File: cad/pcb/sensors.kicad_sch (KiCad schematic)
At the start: 0 parts

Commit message: finish mcu connections
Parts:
- added IC?: MXC4005XC, MXC4005XC, symbol Gyroscope:MXC4005XC
- added IC?: PI4IOE5V96224ZLEX, QFN40P300X600X80-33N, symbol I/O Expander:PI4IOE5V96224ZLEX
- added Q?: 1541201NEA400, 1541201NEA400, symbol Phototransistor:1541201NEA400
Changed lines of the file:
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@@
     (comment 4 "Simon Brenninger")
   )
+  (symbol (lib_id "Phototransistor:1541201NEA400") (at 50.8 49.53 0) (unit 1)
+    (in_bom yes) (on_board yes) (fields_autoplaced)
+    (property "Reference" "Q?" (id 0) (at 54.61 55.6259 0)
+      (effects (font (size 1.27 1.27)) (justify left))
+    )
+    (property "Value" "1541201NEA400" (id 1) (at 54.61 58.1659 0)
+      (effects (font (size 1.27 1.27)) (justify left))
+    )
+    (property "Footprint" "1541201NEA400" (id 2) (at 54.61 60.96 0)
+      (effects (font (size 1.27 1.27)) (justify left) hide)
+    )
+    (property "Datasheet" "https://www.mouser.dk/datasheet/2/445/1541201NEA400-1715480.pdf" (id 3) (at 54.61 63.5 0)
+      (effects (font (size 1.27 1.27)) (justify left) hide)
+    )
+    (property "Description" "WURTH ELEKTRONIK - 1541201NEA400 - Phototransistor, 940 nm, 140 , 150 mW, 2 Pins, 1206, WL-STCB Series" (id 4) (at 54.61 66.04 0)
+      (effects (font (size 1.27 1.27)) (justify left) hide)
+    )
+    (property "Height" "1.2" (id 5) (at 54.61 68.58 0)
+      (effects (font (size 1.27 1.27)) (justify left) hide)
+    )
+    (property "Mouser Part Number" "710-1541201NEA400" (id 6) (at 54.61 71.12 0)
+      (effects (font (size 1.27 1.27)) (justify left) hide)
+    )
+    (property "Mouser Price/Stock" "https://www.mouser.co.uk/ProductDetail/Wurth-Elektronik/1541201NEA400?qs=u16ybLDytRZ%252BRXqtXC1wNA%3D%3D" (id 7) (at 54.61 73.66 0)
+      (effects (font (size 1.27 1.27)) (justify left) hide)
+    )
+    (property "Manufacturer_Name" "Wurth Elektronik" (id 8) (at 54.61 76.2 0)
+      (effects (font (size 1.27 1.27)) (justify left) hide)
+    )
+    (property "Manufacturer_Part_Number" "1541201NEA400" (id 9) (at 54.61 78.74 0)
+      (effects (font (size 1.27 1.27)) (justify left) hide)
+    )
+    (pin "1")
+    (pin "2")
+  )
+  (symbol (lib_id "Gyroscope:MXC4005XC") (at 40.64 93.98 0) (unit 1)
+    (in_bom yes) (on_board yes) (fields_autoplaced)
+    (property "Reference" "IC?" (id 0) (at 53.34 86.36 0))
+    (property "Value" "MXC4005XC" (id 1) (at 53.34 88.9 0))
+    (property "Footprint" "MXC4005XC" (id 2) (at 62.23 91.44 0)
+      (effects (font (size 1.27 1.27)) (justify left) hide)
+    )
+    (property "Datasheet" "https://datasheet.datasheetarchive.com/originals/distributors/Datasheets_SAMA/aa0fcdfc55209a6ab2215b00180fe2f1.pdf" (id 3) (at 62.23 93.98 0)
+      (effects (font (size 1.27 1.27)) (justify left) hide)
+    )
+    (property "Description" "Accelerometers Monolithic and Wafer Level Packaged Three-Axis Accelerometer" (id 4) (at 62.23 96.52 0)
+      (effects (font (size 1.27 1.27)) (justify left) hide)
+    )
+    (property "Height" "0.885" (id 5) (at 62.23 99.06 0)
+      (effects (font (size 1.27 1.27)) (justify left) hide)
+    )
+    (property "Mouser Part Number" "438-MXC4005XC" (id 6) (at 62.23 101.6 0)
+      (effects (font (size 1.27 1.27)) (justify left) hide)
+    )
+    (property "Mouser Price/Stock" "https://www.mouser.co.uk/ProductDetail/MEMSIC/MXC4005XC?qs=RcG8xmE7yp3iyYgWLmAtUw%3D%3D" (id 7) (at 62.23 104.14 0)
+      (effects (font (size 1.27 1.27)) (justify left) hide)
+    )
+    (property "Manufacturer_Name" "MEMSIC" (id 8) (at 62.23 106.68 0)
+      (effects (font (size 1.27 1.27)) (justify left) hide)
+    )
+    (property "Manufacturer_Part_Number" "MXC4005XC" (id 9) (at 62.23 109.22 0)
+      (effects (font (size 1.27 1.27)) (justify left) hide)
+    )
+    (pin "1")
+    (pin "2")
+    (pin "3")
+    (pin "4")
+    (pin "5")
+    (pin "6")
+  )
+  (symbol (lib_id "I{slash}O Expander:PI4IOE5V96224ZLEX") (at 180.34 63.5 0) (unit 1)
+    (in_bom yes) (on_board yes) (fields_autoplaced)
+    (property "Reference" "IC?" (id 0) (at 202.6794 104.14 0)
+      (effects (font (size 1.27 1.27)) (justify left))
+    )
+    (property "Value" "PI4IOE5V96224ZLEX" (id 1) (at 202.6794 106.68 0)
+      (effects (font (size 1.27 1.27)) (justify left))
+    )
+    (property "Footprint" "QFN40P300X600X80-33N" (id 2) (at 209.55 53.34 0)
+      (effects (font (size 1.27 1.27)) (justify left) hide)
+    )
+    (property "Datasheet" "https://www.diodes.com/assets/Datasheets/PI4IOE5V96224.pdf" (id 3) (at 209.55 55.88 0)
+      (effects (font (size 1.27 1.27)) (justify left) hide)
+    )
+    (property "Description" "Interface - I/O Expanders 24-bit I2C-bus I/O Expander" (id 4) (at 209.55 58.42 0)
+      (effects (font (size 1.27 1.27)) (justify left) hide)
+    )
+    (property "Height" "0.8" (id 5) (at 209.55 60.96 0)
+      (effects (font (size 1.27 1.27)) (justify left) hide)
+    )
+    (property "Mouser Part Number" "729-I4IOE5V96224ZLEX" (id 6) (at 209.55 63.5 0)
+      (effects (font (size 1.27 1.27)) (justify left) hide)
+    )
+    (property "Mouser Price/Stock" "https://www.mouser.co.uk/ProductDetail/Diodes-Incorporated/PI4IOE5V96224ZLEX?qs=0lQeLiL1qybZKU%252B6WN8aKg%3D%3D" (id 7) (at 209.55 66.04 0)
+      (effects (font (size 1.27 1.27)) (justify left) hide)
+    )
+    (property "Manufacturer_Name" "Diodes Inc." (id 8) (at 209.55 68.58 0)
+      (effects (font (size 1.27 1.27)) (justify left) hide)
+    )
+    (property "Manufacturer_Part_Number" "PI4IOE5V96224ZLEX" (id 9) (at 209.55 71.12 0)
+      (effects (font (size 1.27 1.27)) (justify left) hide)
+    )
+    (pin "1")
+    (pin "10")
+    (pin "11")
+    (pin "12")
+    (pin "13")
+    (pin "14")
+    (pin "15")
+    (pin "16")
+    (pin "17")
+    (pin "18")
+    (pin "19")
+    (pin "2")
+    (pin "20")
+    (pin "21")
+    (pin "22")
+    (pin "23")
+    (pin "24")
+    (pin "25")
+    (pin "26")
+    (pin "27")
+    (pin "28")
+    (pin "29")
+    (pin "3")
+    (pin "30")
+    (pin "31")
+    (pin "32")
+    (pin "33")
+    (pin "4")
+    (pin "5")
+    (pin "6")
+    (pin "7")
+    (pin "8")
+    (pin "9")
+  )
 )

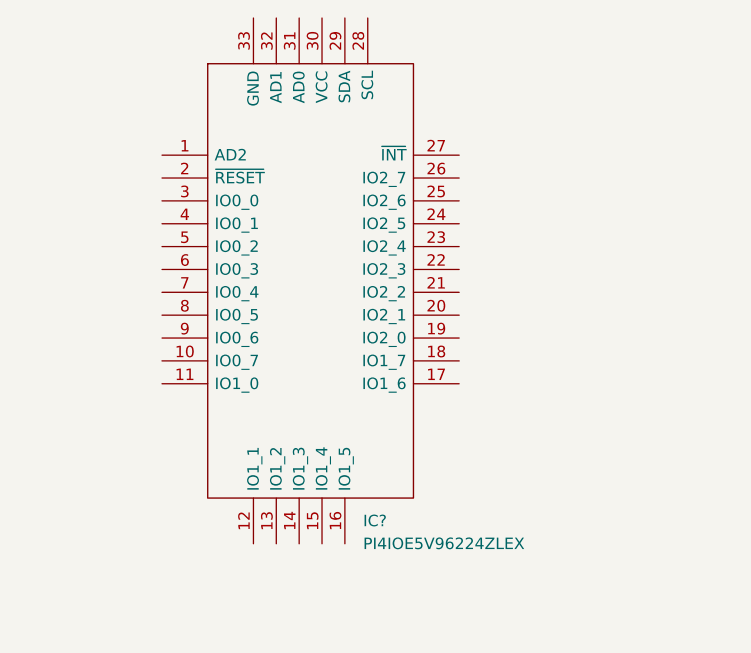
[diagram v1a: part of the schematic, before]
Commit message: changed MCU package
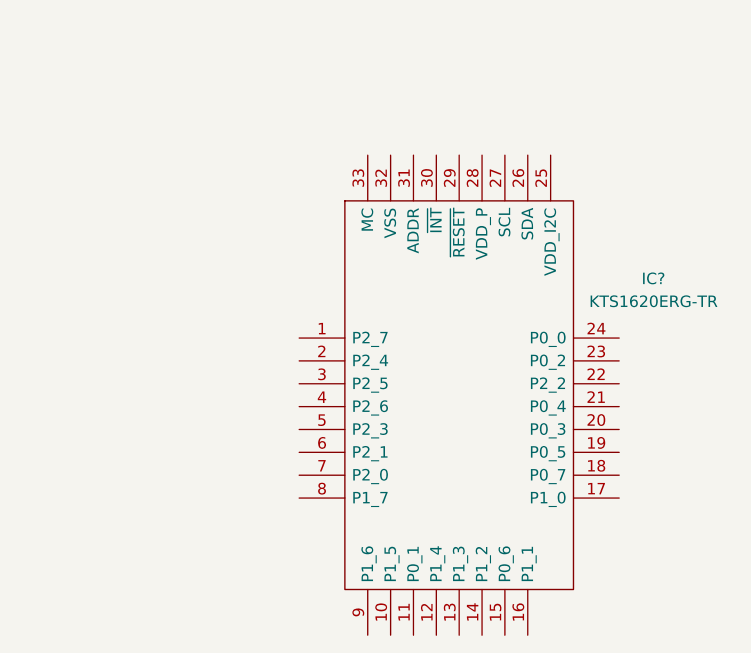
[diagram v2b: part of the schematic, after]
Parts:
- removed IC?: PI4IOE5V96224ZLEX, QFN40P300X600X80-33N, symbol I/O Expander:PI4IOE5V96224ZLEX
- added IC?: KTS1620ERG-TR, QFN50P500X500X80-33N-D, symbol I/O-Expander:KTS1620ERG-TR
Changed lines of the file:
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@@
     (pin "6")
   )
-  (symbol (lib_id "I{slash}O Expander:PI4IOE5V96224ZLEX") (at 180.34 63.5 0) (unit 1)
+  (symbol (lib_id "I{slash}O-Expander:KTS1620ERG-TR") (at 195.58 83.82 0) (unit 1)
     (in_bom yes) (on_board yes) (fields_autoplaced)
-    (property "Reference" "IC?" (id 0) (at 202.6794 104.14 0)
-      (effects (font (size 1.27 1.27)) (justify left))
-    )
-    (property "Value" "PI4IOE5V96224ZLEX" (id 1) (at 202.6794 106.68 0)
-      (effects (font (size 1.27 1.27)) (justify left))
-    )
-    (property "Footprint" "QFN40P300X600X80-33N" (id 2) (at 209.55 53.34 0)
+    (property "Reference" "IC?" (id 0) (at 234.95 77.2412 0))
+    (property "Value" "KTS1620ERG-TR" (id 1) (at 234.95 79.7812 0))
+    (property "Footprint" "QFN50P500X500X80-33N-D" (id 2) (at 227.33 68.58 0)
       (effects (font (size 1.27 1.27)) (justify left) hide)
     )
-    (property "Datasheet" "https://www.diodes.com/assets/Datasheets/PI4IOE5V96224.pdf" (id 3) (at 209.55 55.88 0)
+    (property "Datasheet" "" (id 3) (at 227.33 71.12 0)
       (effects (font (size 1.27 1.27)) (justify left) hide)
     )
-    (property "Description" "Interface - I/O Expanders 24-bit I2C-bus I/O Expander" (id 4) (at 209.55 58.42 0)
+    (property "Description" "Interface - I/O Expanders Low Voltage 24-bit I2C-bus I/O Expander" (id 4) (at 227.33 73.66 0)
       (effects (font (size 1.27 1.27)) (justify left) hide)
     )
-    (property "Height" "0.8" (id 5) (at 209.55 60.96 0)
+    (property "Height" "0.8" (id 5) (at 227.33 76.2 0)
       (effects (font (size 1.27 1.27)) (justify left) hide)
     )
-    (property "Mouser Part Number" "729-I4IOE5V96224ZLEX" (id 6) (at 209.55 63.5 0)
+    (property "Mouser2 Part Number" "" (id 6) (at 227.33 78.74 0)
       (effects (font (size 1.27 1.27)) (justify left) hide)
     )
-    (property "Mouser Price/Stock" "https://www.mouser.co.uk/ProductDetail/Diodes-Incorporated/PI4IOE5V96224ZLEX?qs=0lQeLiL1qybZKU%252B6WN8aKg%3D%3D" (id 7) (at 209.55 66.04 0)
+    (property "Mouser2 Price/Stock" "" (id 7) (at 227.33 81.28 0)
       (effects (font (size 1.27 1.27)) (justify left) hide)
     )
-    (property "Manufacturer_Name" "Diodes Inc." (id 8) (at 209.55 68.58 0)
+    (property "Manufacturer_Name" "Kinetic Technologies" (id 8) (at 227.33 83.82 0)
       (effects (font (size 1.27 1.27)) (justify left) hide)
     )
-    (property "Manufacturer_Part_Number" "PI4IOE5V96224ZLEX" (id 9) (at 209.55 71.12 0)
+    (property "Manufacturer_Part_Number" "KTS1620ERG-TR" (id 9) (at 227.33 86.36 0)
       (effects (font (size 1.27 1.27)) (justify left) hide)
     )

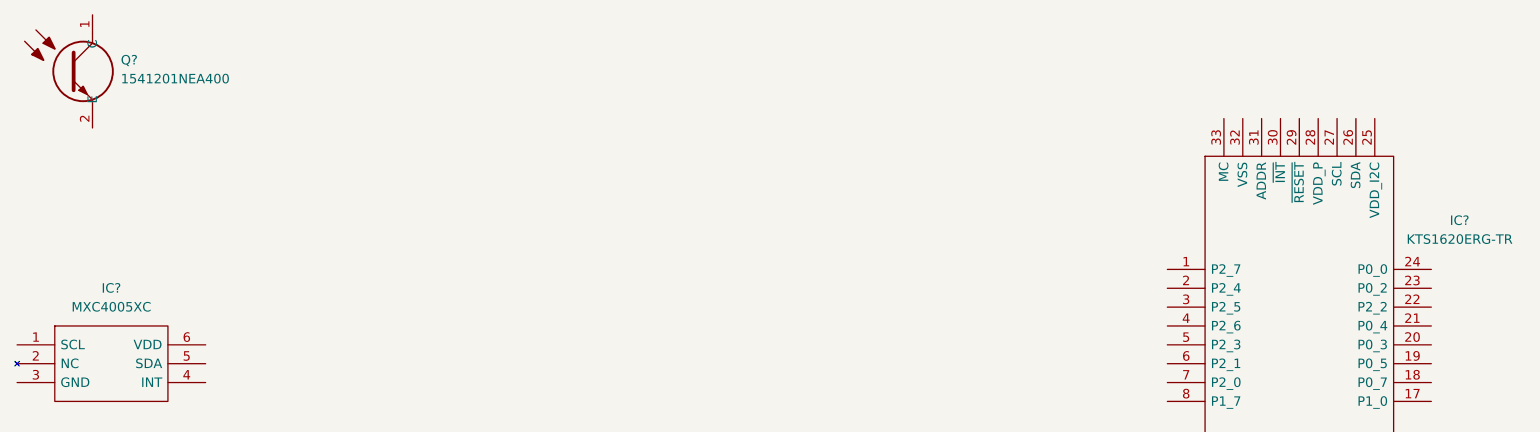
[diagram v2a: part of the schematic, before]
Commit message: add charging & preotection circuit
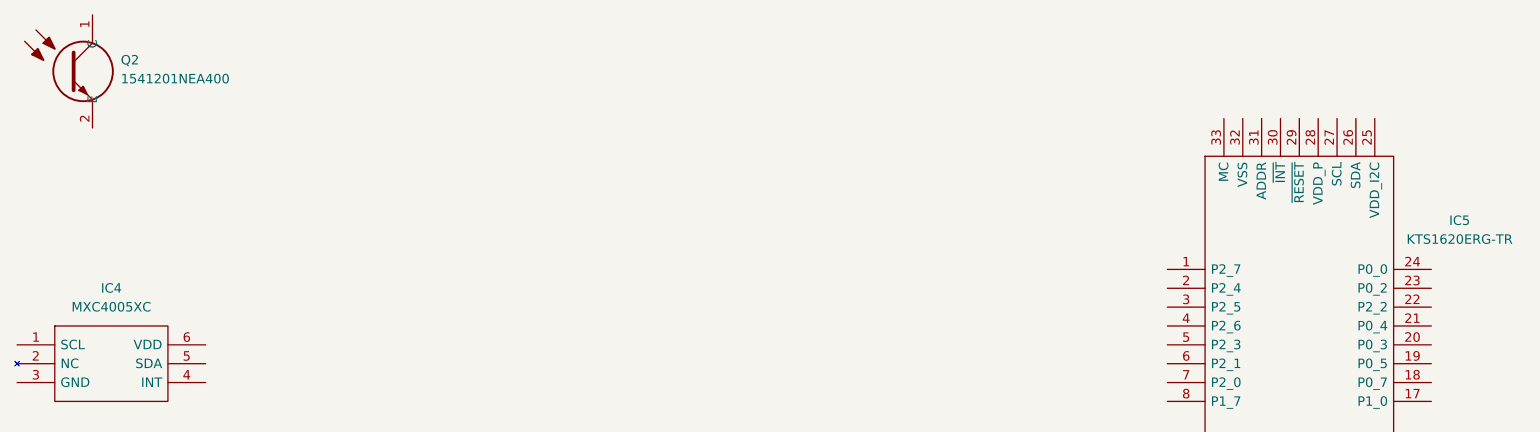
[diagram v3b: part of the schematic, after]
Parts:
- gave numbers to parts that had none: 3
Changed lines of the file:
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@@
   (symbol (lib_id "Phototransistor:1541201NEA400") (at 50.8 49.53 0) (unit 1)
     (in_bom yes) (on_board yes) (fields_autoplaced)
-    (property "Reference" "Q?" (id 0) (at 54.61 55.6259 0)
+    (property "Reference" "Q2" (id 0) (at 54.61 55.6259 0)
       (effects (font (size 1.27 1.27)) (justify left))
     )
@@
   (symbol (lib_id "Gyroscope:MXC4005XC") (at 40.64 93.98 0) (unit 1)
     (in_bom yes) (on_board yes) (fields_autoplaced)
-    (property "Reference" "IC?" (id 0) (at 53.34 86.36 0))
+    (property "Reference" "IC4" (id 0) (at 53.34 86.36 0))
     (property "Value" "MXC4005XC" (id 1) (at 53.34 88.9 0))
     (property "Footprint" "MXC4005XC" (id 2) (at 62.23 91.44 0)
@@
   (symbol (lib_id "I{slash}O-Expander:KTS1620ERG-TR") (at 195.58 83.82 0) (unit 1)
     (in_bom yes) (on_board yes) (fields_autoplaced)
-    (property "Reference" "IC?" (id 0) (at 234.95 77.2412 0))
+    (property "Reference" "IC5" (id 0) (at 234.95 77.2412 0))
     (property "Value" "KTS1620ERG-TR" (id 1) (at 234.95 79.7812 0))
     (property "Footprint" "QFN50P500X500X80-33N-D" (id 2) (at 227.33 68.58 0)

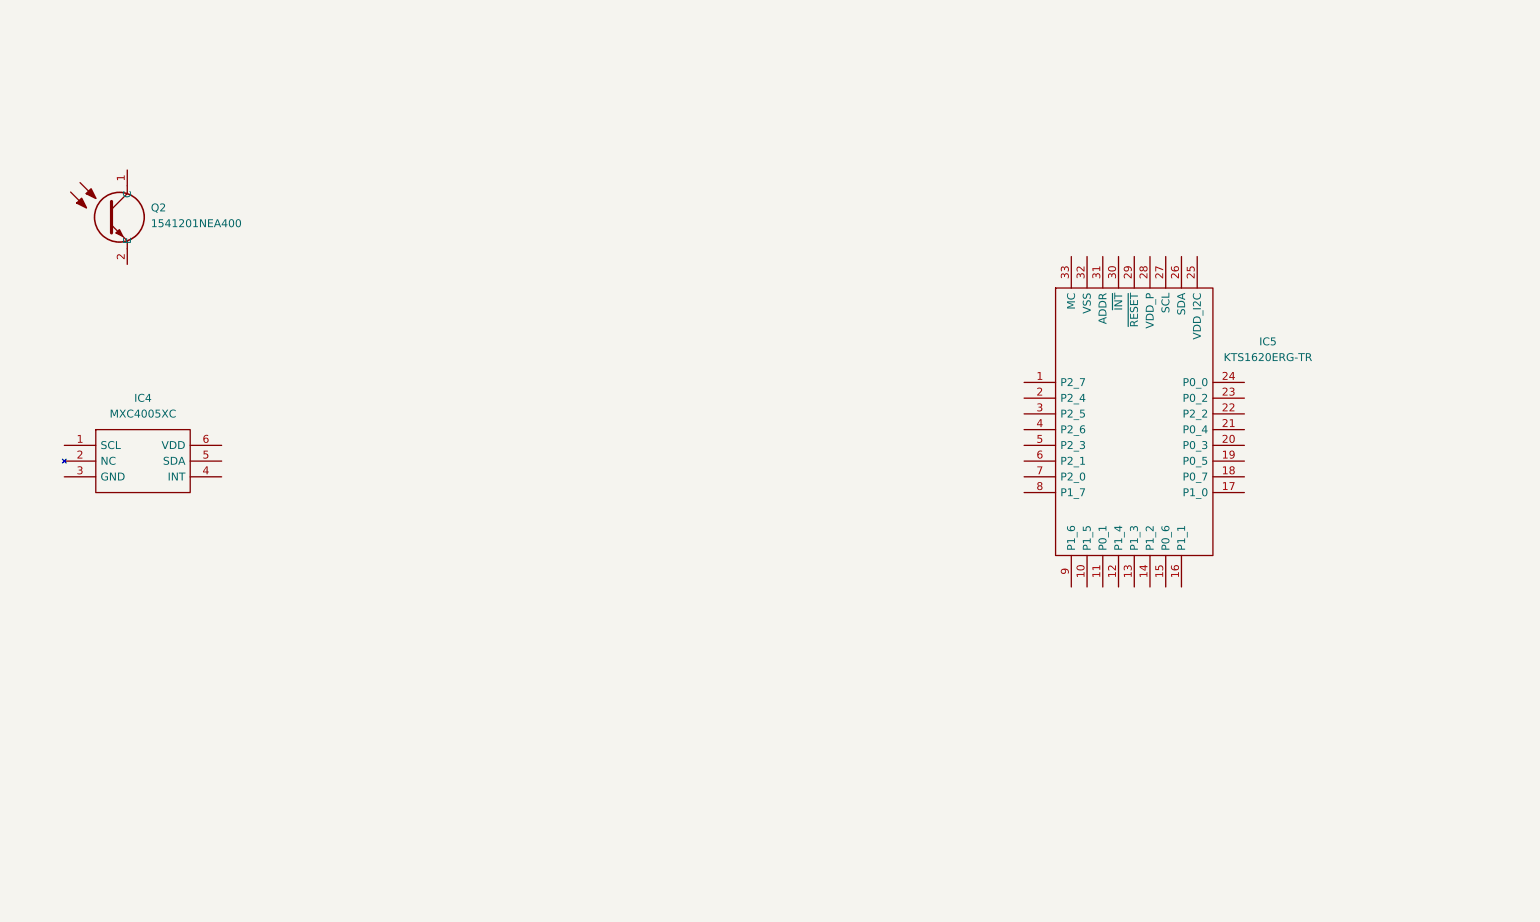
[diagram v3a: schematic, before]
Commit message: add dc-dc converter, add sensors
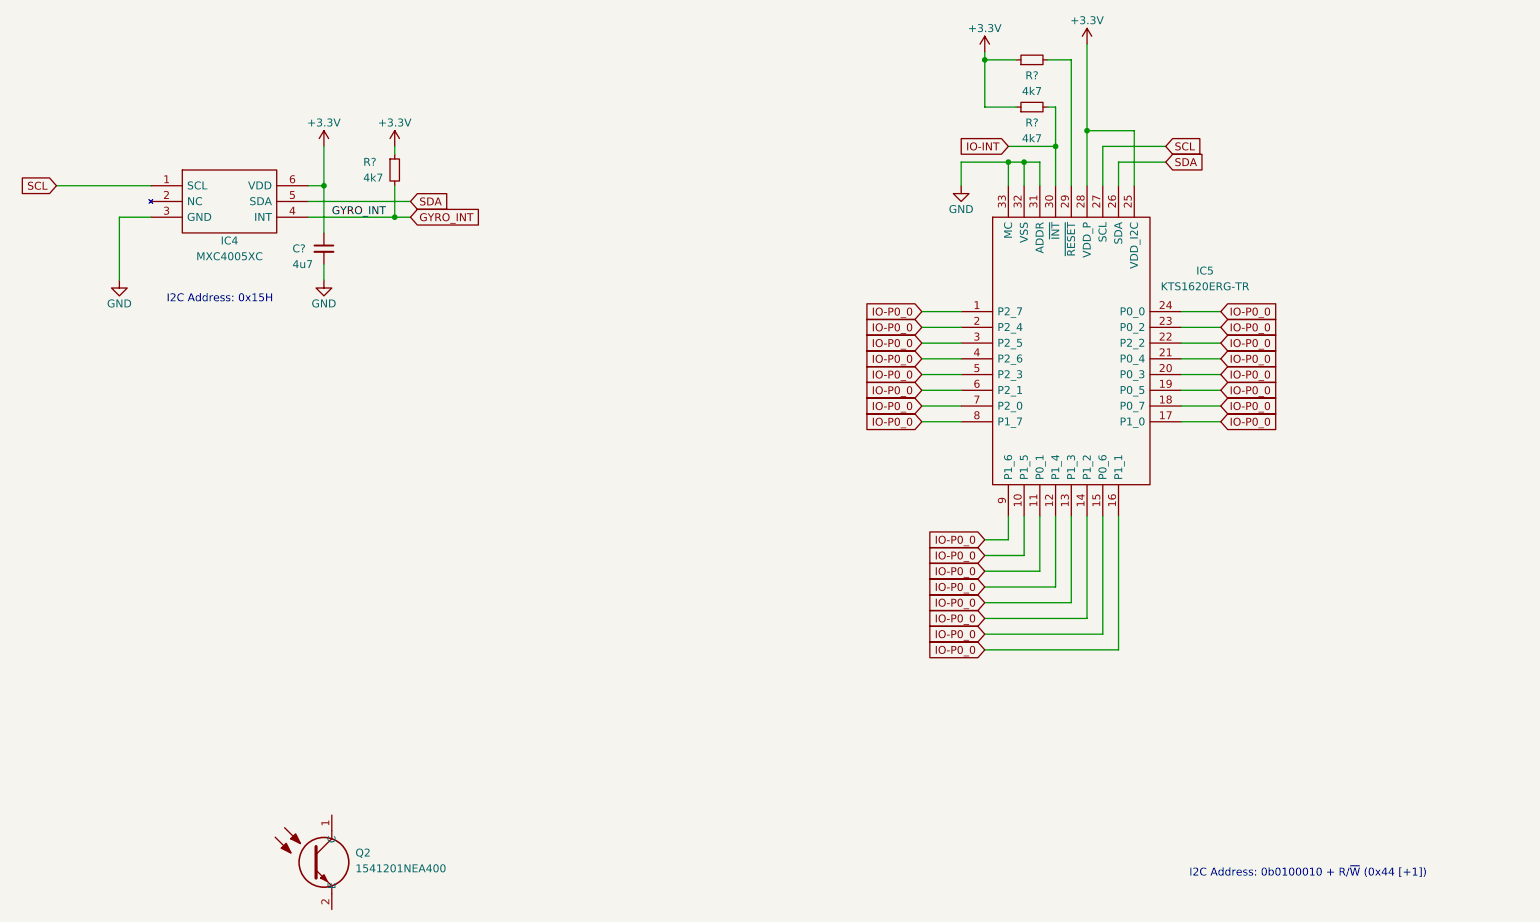
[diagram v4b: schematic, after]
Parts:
- added C?: 4u7, symbol Device:C_Small
- added R? (x3): 4k7, symbol Device:R_Small
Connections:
- net SCL: now reaches IC4.1 (SCL)
- net SCL: now also IC5.27 (SCL)
- net GND: now reaches IC4.3 (GND)
- net GND: now also IC5.31 (ADDR), IC5.32 (VSS), IC5.33 (MC), C?.2
- net GYRO_INT: now reaches IC4.4 (INT)
- net GYRO_INT: now also R?.2
- net SDA: now reaches IC4.5 (SDA)
- net SDA: now also IC5.26 (SDA)
- net +3.3V: now reaches IC4.6 (VDD)
- net +3.3V: now also IC5.25 (VDD_I2C), IC5.28 (VDD_P), C?.1, R?.1, R?.1, R?.1
- net IO-P0_0: now reaches IC5.1 (P2_7)
- net IO-P0_0: now also IC5.10 (P1_5), IC5.11 (P0_1), IC5.12 (P1_4), IC5.13 (P1_3), IC5.14 (P1_2), IC5.15 (P0_6), IC5.16 (P1_1), IC5.17 (P1_0), IC5.18 (P0_7), IC5.19 (P0_5), IC5.2 (P2_4), IC5.20 (P0_3), IC5.21 (P0_4), IC5.22 (P2_2), IC5.23 (P0_2), IC5.24 (P0_0), IC5.3 (P2_5), IC5.4 (P2_6), IC5.5 (P2_3), IC5.6 (P2_1), IC5.7 (P2_0), IC5.8 (P1_7), IC5.9 (P1_6)
- net at IC5.29 (~{RESET}): now also R?.2
- net IO-INT: now reaches IC5.30 (~{INT})
- net IO-INT: now also R?.2
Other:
- note added: "I2C Address: 0b0100010 + R/~{W} (0x44 [+1])"
- note added: "I2C Address: 0x15H"
- moved on the sheet: IC4, IC5, Q2
